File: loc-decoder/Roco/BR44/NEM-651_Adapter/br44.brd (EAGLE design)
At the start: 38 x 17 mm, 8 parts

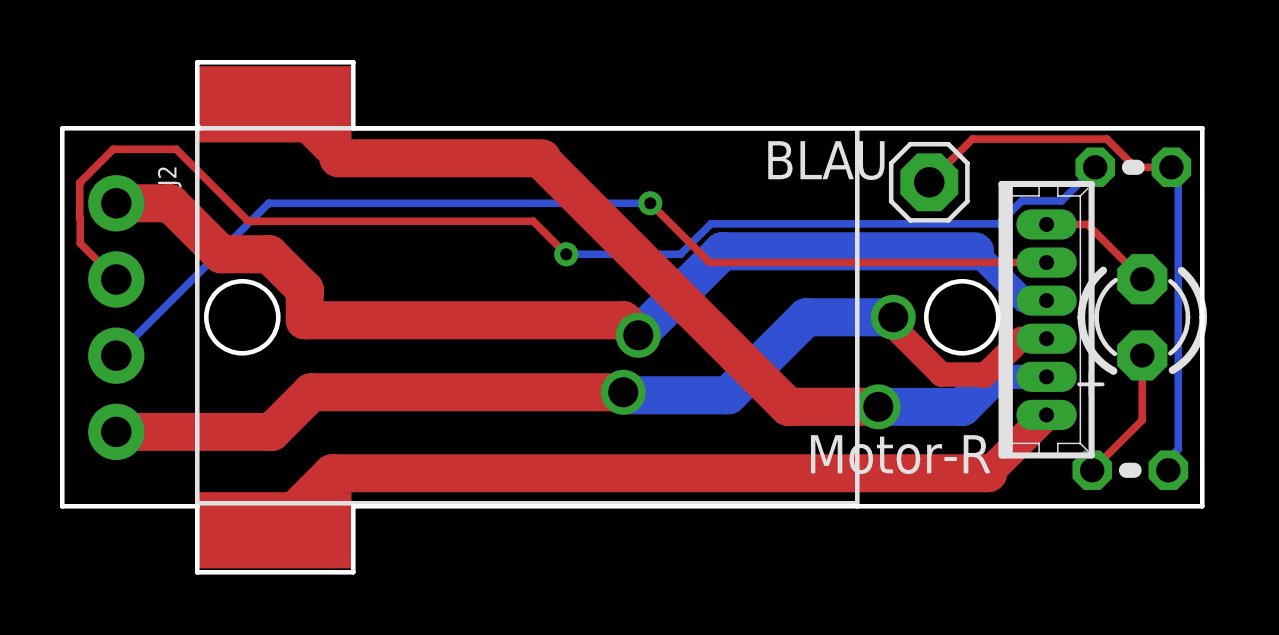
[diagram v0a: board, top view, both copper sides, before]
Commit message: BR44 nut soldermask correction
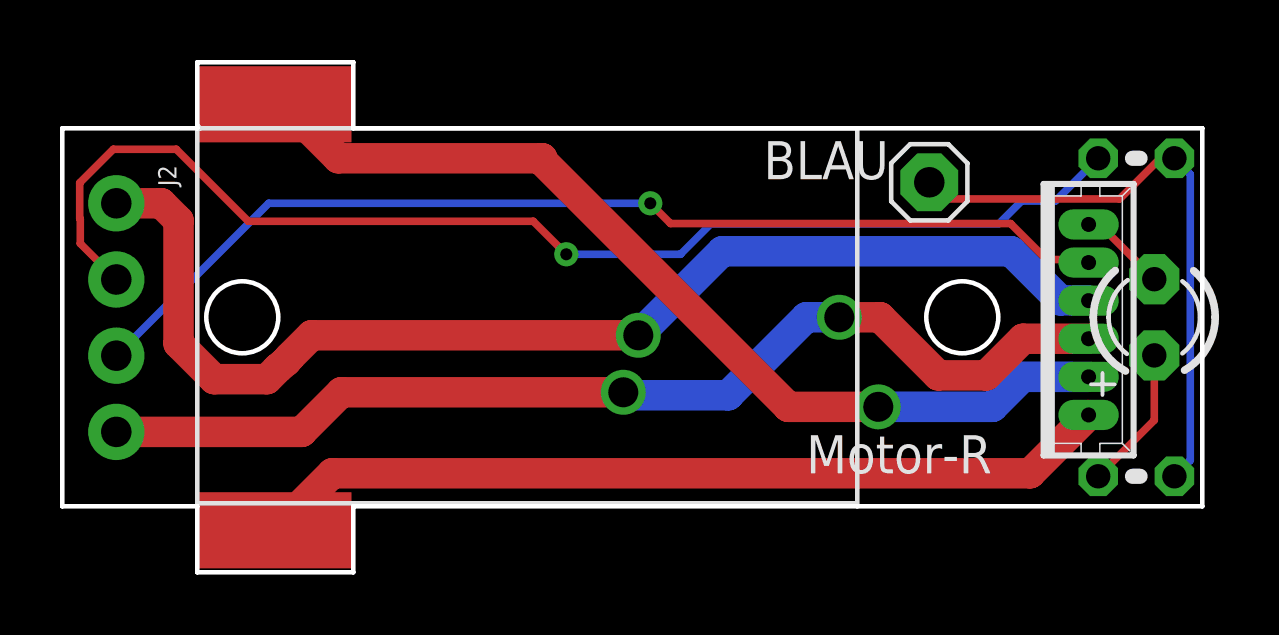
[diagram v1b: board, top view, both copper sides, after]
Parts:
- moved U$1 1.40 mm to (34.2, 8.42)
- moved LED2 0.40 mm to (36.4, 8.50)
- moved R3 0.32 mm to (35.8, 13.8)
- moved R4 0.28 mm to (35.8, 3.20)
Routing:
- net N$4: track 35.3 -> 39.7 mm
- net N$2: track 30.4 -> 31.8 mm
- net N$1: track 27.3 -> 28.7 mm
- net N$8: track 33.9 -> 35.3 mm
- net N$3: track 34.2 -> 35.4 mm
- net N$9: track 3.95 -> 2.95 mm
- net N$5: track 19.4 -> 20.0 mm
